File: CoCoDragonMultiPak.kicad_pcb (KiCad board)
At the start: 2 copper layers, 137.7 x 171.2 mm, 57 parts, among them IC1 74LS245DWR, IC11 74LS153DR, IC2 74LS367ADR, IC3 74LS367ADR, IC4 74LS367ADR, IC5 74LS367ADR, IC6 74LS367ADR, IC7 74LS374DWR, IC8 74LS368AD, IC9 74LS139ADR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

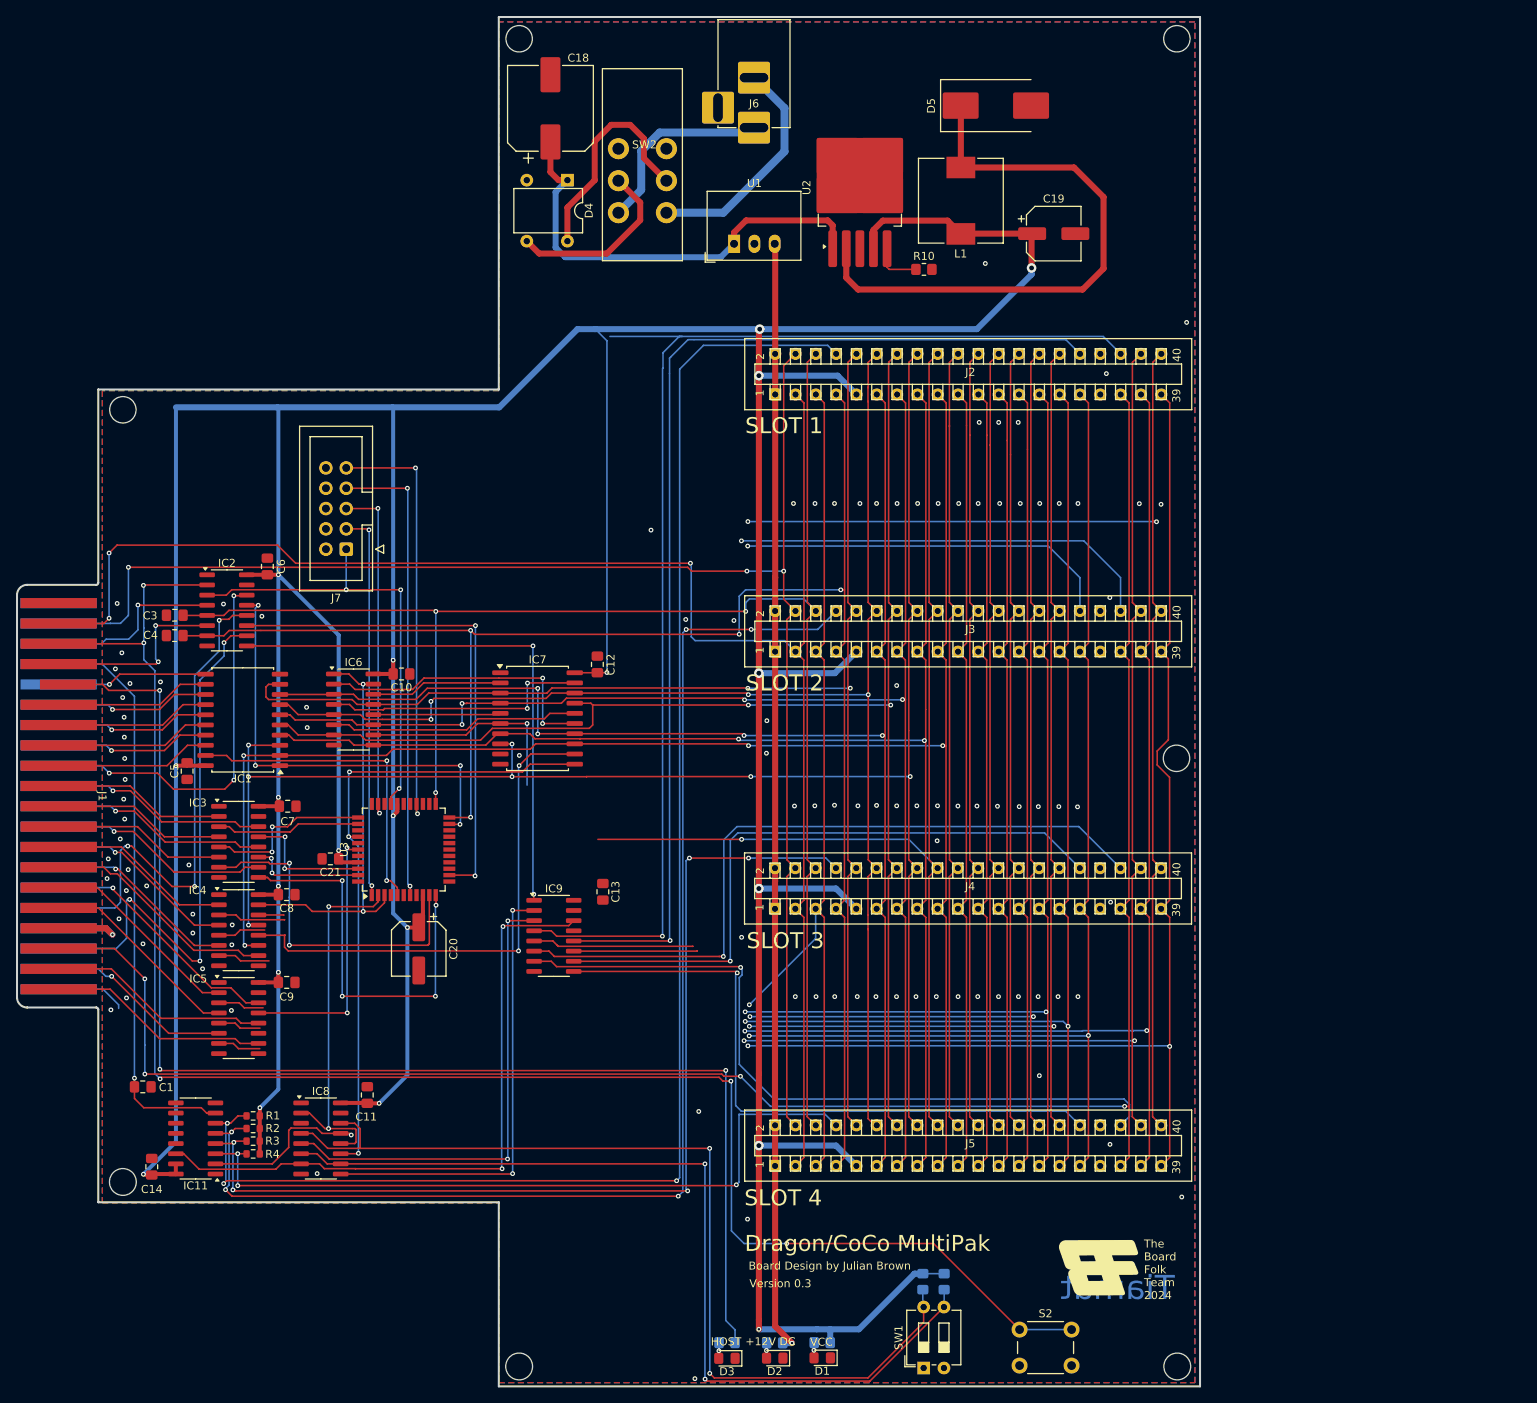
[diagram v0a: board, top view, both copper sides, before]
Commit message: convert to ATF1508
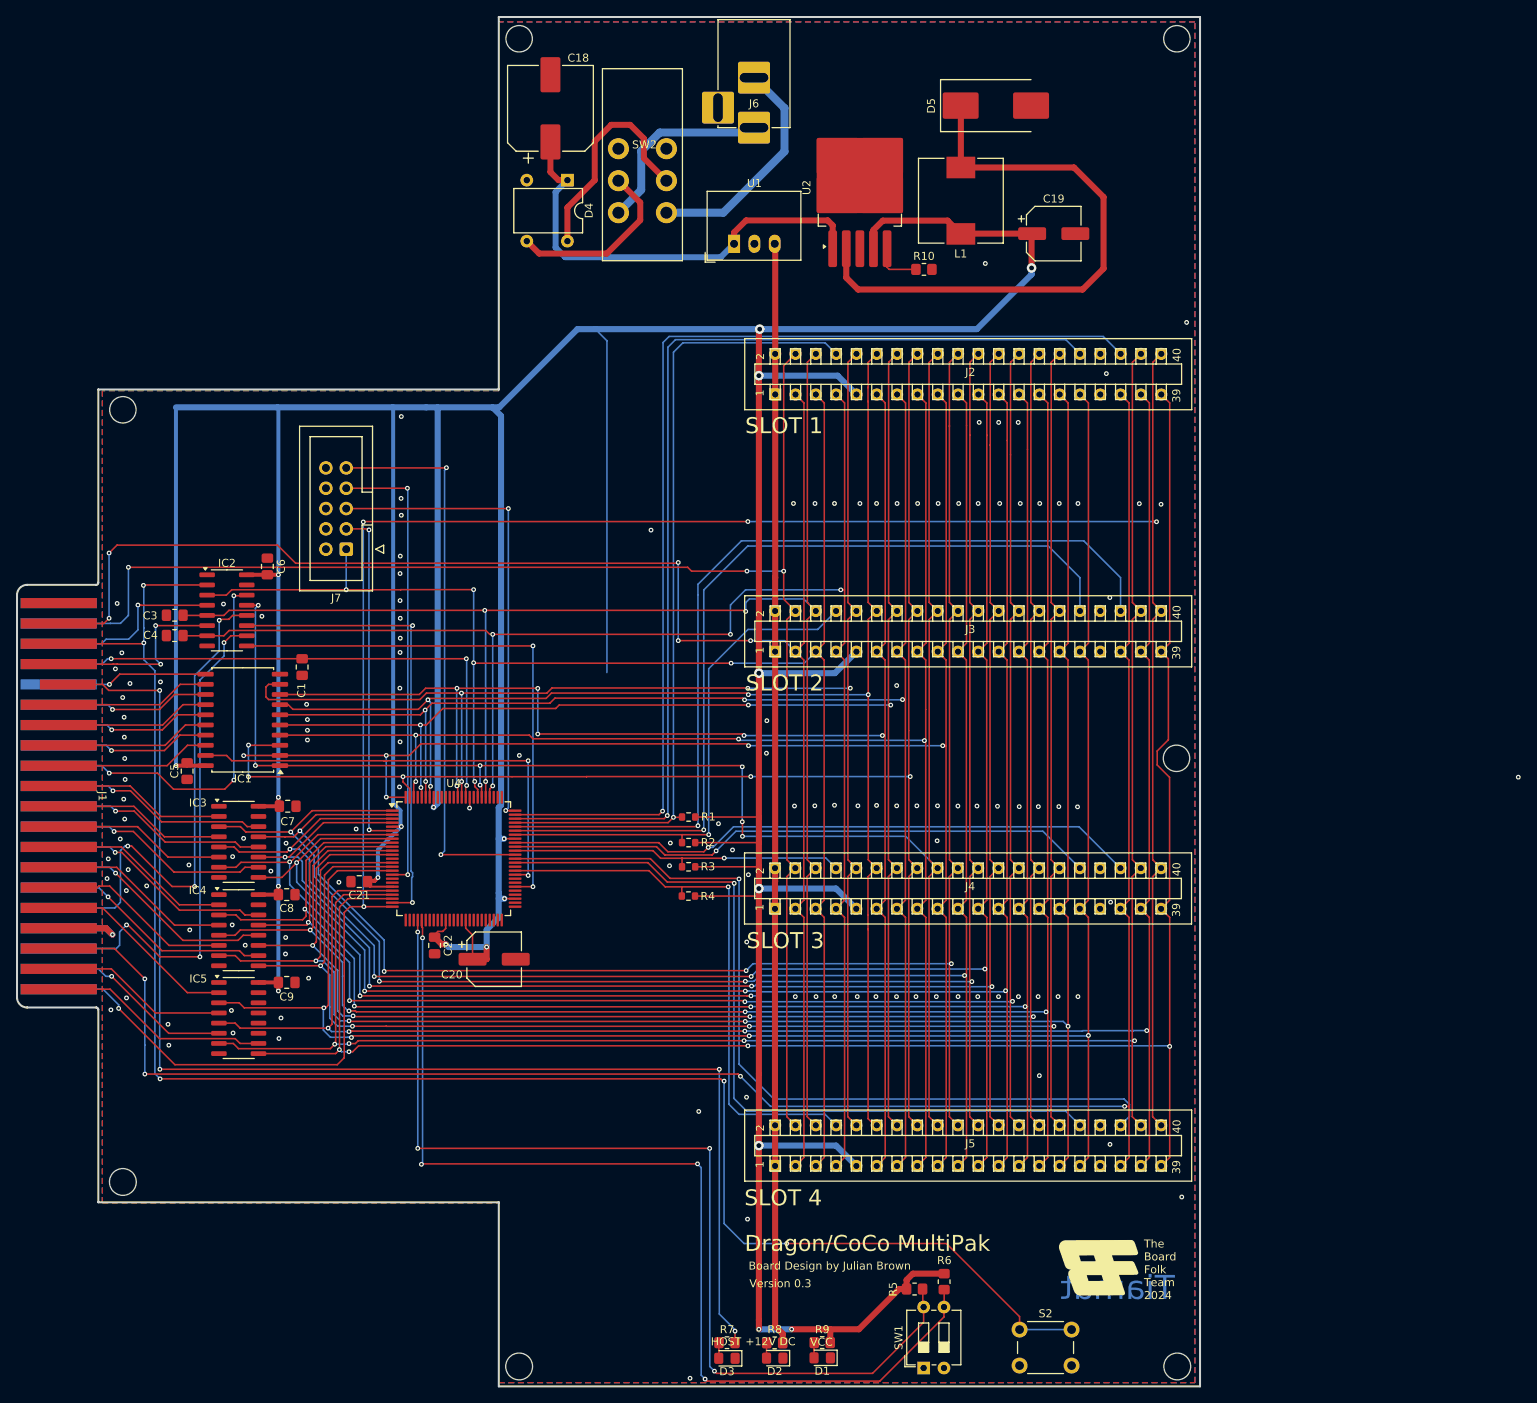
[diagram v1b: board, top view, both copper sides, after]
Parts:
- removed C10, C11, C12, C13, C14: 100nF, Capacitor_SMD:C_0805_2012Metric_Pad1.18x1.45mm_HandSolder
- removed IC11: 74LS153DR, Package_SO:SOIC-16_3.9x9.9mm_P1.27mm
- removed IC6: 74LS367ADR, Package_SO:SOIC-16_3.9x9.9mm_P1.27mm
- removed IC7: 74LS374DWR, Package_SO:SOIC-20W_7.5x12.8mm_P1.27mm
- removed IC8: 74LS368AD, Package_SO:SOIC-16_3.9x9.9mm_P1.27mm
- removed IC9: 74LS139ADR, Package_SO:SOIC-16_3.9x9.9mm_P1.27mm
- removed U3: ATF1504AS-xAx44, Package_QFP:TQFP-44_10x10mm_P0.8mm
- added C22: 100nF, Capacitor_SMD:C_0805_2012Metric_Pad1.18x1.45mm_HandSolder, F.Cu at (85.6, 164.5)
- added U4: ATF1508AS-15AU100, Package_QFP:LQFP-100_14x14mm_P0.5mm, F.Cu at (88.0, 153.6)
- R5, R6, R7, R8, R9: moved to F.Cu
- moved R1 66.0 mm to (117.4, 148.4)
- moved R2 65.1 mm to (117.4, 151.6)
- moved R3 64.3 mm to (117.4, 154.7)
- moved R4 63.2 mm to (117.4, 158.3)
- moved C1 56.1 mm to (69.1, 129.7), turned to -90 degrees
- moved C20 9.51 mm to (93.1, 166.2), turned to 0 degrees
- moved C21 4.60 mm to (76.2, 156.5)
- moved R5 1.38 mm to (145.6, 207.4), turned to 180 degrees
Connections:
- IC1 pad 19: /~{ENBUS} -> /~{IOW}
- IC4 pad 10: /A8 -> /A11
- IC4 pad 11: /ID7 -> /IA9
- IC4 pad 12: /CK3 -> /A9
- IC4 pad 13: /ID6 -> /IA7
- IC4 pad 14: /CK2 -> /A7
- IC4 pad 15: /~{ENREAD} -> GND
- IC4 pad 4: /A7 -> /A8
- IC4 pad 5: /IA7 -> /IA8
- IC4 pad 6: /A9 -> /A10
- IC4 pad 7: /IA9 -> /IA10
- IC4 pad 9: /IA8 -> /IA11
- IC5 pad 11: /IA13 -> unconnected-(IC5-O5b-Pad11)
- IC5 pad 12: /A13 -> unconnected-(IC5-I5-Pad12)
- IC5 pad 13: /IA11 -> unconnected-(IC5-O6b-Pad13)
- IC5 pad 14: /A11 -> unconnected-(IC5-I6-Pad14)
- IC5 pad 2: /A10 -> /A12
- IC5 pad 3: /IA10 -> /IA12
- IC5 pad 4: /A12 -> /A13
- IC5 pad 5: /IA12 -> /IA13
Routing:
- net /~{SLEN}: track 159.4 -> 311.6 mm, vias 2 -> 5
- net /IA6: track 107.5 -> 228.0 mm, vias 0 -> 4
- net /IA7: track 105.1 -> 219.4 mm, vias 0 -> 4
- net /REGC0: track 112.9 -> 0.00 mm, vias 2 -> 0
- net /IA0: track 117.2 -> 218.9 mm, vias 0 -> 4
- net /IA3: track 113.5 -> 214.8 mm, vias 2 -> 4
- net /IA2: track 120.4 -> 220.7 mm, vias 2 -> 4
- net /REGS1: track 96.4 -> 0.00 mm, vias 4 -> 0
- net /~{CART2}: track 159.6 -> 64.9 mm, vias 5 -> 1
- net /IA1: track 115.6 -> 210.2 mm, vias 2 -> 4
- net /IA8: track 136.9 -> 229.2 mm, vias 2 -> 4
- net /~{CART1}: track 191.6 -> 100.7 mm, vias 3 -> 1
- net /IA13: track 149.7 -> 240.4 mm, vias 2 -> 4
- net /IA12: track 146.9 -> 236.2 mm, vias 2 -> 4
- net /IA10: track 145.5 -> 232.9 mm, vias 2 -> 4
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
